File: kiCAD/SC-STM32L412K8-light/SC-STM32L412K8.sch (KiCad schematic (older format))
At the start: 66 parts, among them J1 usb, J10 Buzzer, J11 Vibro, J12 +3v, J13 +vibro, J2 +29.6 SiPM, J3 TxD (20), J4 RxD (19), J5 SWDIO, J6 SWCLK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

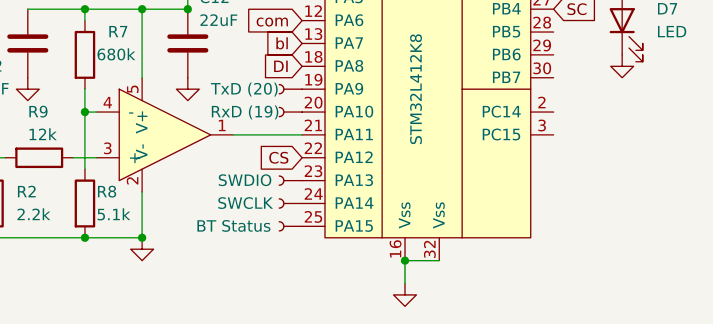
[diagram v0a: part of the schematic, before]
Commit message: modified:   kiCAD/SC-STM32L412K8-light/SC-STM32L412K8.sch 	modified:   kiCAD/SC-STM32L412K8-light/SC-STM32L412K8.sch-bak
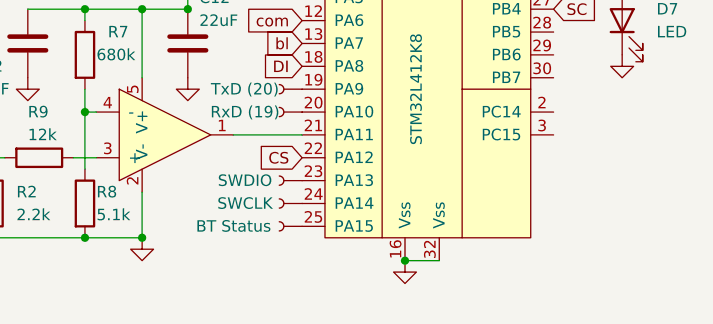
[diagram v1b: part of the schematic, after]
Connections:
- wire segments 124 -> 123
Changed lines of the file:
@@
 L power:GND #PWR012
 U 1 1 60366E3E
-P 7300 5700
-F 0 "#PWR012" H 7300 5450 50  0001 C CNN
-F 1 "GND" H 7305 5527 50  0001 C CNN
-F 2 "" H 7300 5700 50  0001 C CNN
-F 3 "" H 7300 5700 50  0001 C CNN
-	1    7300 5700
+P 7300 5600
+F 0 "#PWR012" H 7300 5350 50  0001 C CNN
+F 1 "GND" H 7305 5427 50  0001 C CNN
+F 2 "" H 7300 5600 50  0001 C CNN
+F 3 "" H 7300 5600 50  0001 C CNN
+	1    7300 5600
 	1    0    0    -1
 $EndComp
 Wire Wire Line
 	7450 5600 7300 5600
-Wire Wire Line
-	7300 5600 7300 5700
-Connection ~ 7300 5600
 $Comp
 L Device:L L4
@@
 Text GLabel 6850 5150 0    50   Input ~ 0
 CS
+Connection ~ 7300 5600
 $EndSCHEMATC

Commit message: изменено:      Android/AndroidDoZer/app/src/main/java/ru/starline/dozer/FullscreenActivity.java 	изменено:      Android/AndroidDoZer/app/src/main/res/values/strings.xml 	изменено:      kiCAD/SC-STM32L412K8-light/SC-STM32L412K8.sch 	изменено:      kiCAD/SC-STM32L412K8-light/SC-STM32L412K8.sch-bak 	изменено:      stm32Cube/STM32L412K8code/Core/Src/main.c 	изменено:      stm32Cube/STM32L412K8code/Core/Src/stm32l4xx_it.c 	изменено:      stm32Cube/STM32L412K8code/Release/Core/Src/main.o 	изменено:      stm32Cube/STM32L412K8code/Release/Core/Src/main.su 	изменено:      stm32Cube/STM32L412K8code/Release/Core/Src/stm32l4xx_it.o 	изменено:      stm32Cube/STM32L412K8code/Release/STM32L412K8.bin 	изменено:      stm32Cube/STM32L412K8code/Release/STM32L412K8.elf 	изменено:      stm32Cube/STM32L412K8code/Release/STM32L412K8.list 	изменено:      stm32Cube/STM32L412K8code/Release/STM32L412K8.map 	изменено:      stm32Cube/STM32L412K8code/STM32L412K8.ioc
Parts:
- Q1, Q2: value IRLML6344 -> IRLML0060RTPbF
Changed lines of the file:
@@
 P 4550 4350
 F 0 "Q1" H 4756 4396 50  0000 L CNN
-F 1 "IRLML6344" H 4756 4305 50  0000 L CNN
+F 1 "IRLML0060RTPbF" H 4756 4305 50  0000 L CNN
 F 2 "Package_TO_SOT_SMD:SOT-23" H 4750 4275 50  0001 L CIN
 F 3 "https://www.fairchildsemi.com/datasheets/2N/2N7002.pdf" H 4550 4350 50  0001 L CNN
@@
 P 4550 5200
 F 0 "Q2" H 4756 5246 50  0000 L CNN
-F 1 "IRLML6344" H 4756 5155 50  0000 L CNN
+F 1 "IRLML0060RTPbF" H 4756 5155 50  0000 L CNN
 F 2 "Package_TO_SOT_SMD:SOT-23" H 4750 5125 50  0001 L CIN
 F 3 "https://www.fairchildsemi.com/datasheets/2N/2N7002.pdf" H 4550 5200 50  0001 L CNN

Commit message: modified:   kiCAD/SC-STM32L412K8-light/SC-STM32L412K8.kicad_pcb 	modified:   kiCAD/SC-STM32L412K8-light/SC-STM32L412K8.kicad_pcb-bak 	modified:   kiCAD/SC-STM32L412K8-light/SC-STM32L412K8.sch 	modified:   kiCAD/SC-STM32L412K8-light/SC-STM32L412K8.sch-bak
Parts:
- L1: value LQM21FN100N -> L1 LQM21FN100N
- L2: value LQH31MN220J03L -> L2 LQH31MN220J03L
- L3: value MLZ2012M470WT000 -> L3 MLZ2012M470WT000
- L4: value MLZ2012M470WT000 -> L4 MLZ2012M470WT000
- R17: value 10M -> 30M
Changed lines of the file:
@@
 P 4600 1300
 F 0 "L2" V 4700 1300 50  0000 C CNN
-F 1 "LQH31MN220J03L" V 4800 1300 50  0000 C CNN
+F 1 "L2 LQH31MN220J03L" V 5300 1350 50  0000 C CNN
 F 2 "Inductor_SMD:L_1210_3225Metric" H 4600 1300 50  0001 C CNN
 F 3 "~" H 4600 1300 50  0001 C CNN
@@
 U 1 1 6037B2E7
 P 7500 3550
-F 0 "L4" H 7450 3900 50  0000 L CNN
-F 1 "MLZ2012M470WT000" H 7450 3800 50  0000 L CNN
+F 0 "L4" H 7350 3550 50  0000 L CNN
+F 1 "L4 MLZ2012M470WT000" H 6800 6500 50  0000 L CNN
 F 2 "Inductor_SMD:L_0805_2012Metric" H 7500 3550 50  0001 C CNN
 F 3 "~" H 7500 3550 50  0001 C CNN
@@
 P 5000 3450
 F 0 "U3" H 5050 2950 50  0000 L CNN
-F 1 "MCP73831" H 4900 2850 50  0000 L CNN
+F 1 "MCP73831" H 5000 2850 50  0000 L CNN
 F 2 "Package_TO_SOT_SMD:TSOT-23-5" H 5000 2950 50  0001 C CNN
 F 3 "http://cds.linear.com/docs/en/datasheet/405442xf.pdf" H 5000 3350 50  0001 C CNN
@@
 U 1 1 60436BF5
 P 4100 1300
-F 0 "L1" V 4300 1450 50  0000 C CNN
-F 1 "LQM21FN100N" V 4200 1200 50  0000 C CNN
+F 0 "L1" V 4200 1300 50  0000 C CNN
+F 1 "L1 LQM21FN100N" V 4800 0   50  0000 C CNN
 F 2 "Inductor_SMD:L_0805_2012Metric" H 4100 1300 50  0001 C CNN
 F 3 "~" H 4100 1300 50  0001 C CNN
@@
 U 1 1 60437DE2
 P 5600 1300
-F 0 "L3" V 5500 1300 50  0000 C CNN
-F 1 "MLZ2012M470WT000" V 5750 1000 50  0000 C CNN
+F 0 "L3" V 5700 1300 50  0000 C CNN
+F 1 "L3 MLZ2012M470WT000" V 6300 650 50  0000 C CNN
 F 2 "Inductor_SMD:L_0805_2012Metric" H 5600 1300 50  0001 C CNN
 F 3 "MLZ2012M470WT000" H 5600 1300 50  0001 C CNN
@@
 P 6500 1300
 F 0 "J2" H 6442 1075 50  0001 C CNN
-F 1 "+29.6 SiPM" H 6600 1400 50  0000 C CNN
+F 1 "+29.6 SiPM" H 6350 1400 50  0000 C CNN
 F 2 "My-library:SMD-CONN" H 6500 1300 50  0001 C CNN
 F 3 "~" H 6500 1300 50  0001 C CNN
@@
 Wire Wire Line
 	5500 5150 5500 5100
-Text Notes 5400 750  0    50   ~ 0
+Text Notes 4150 750  0    50   ~ 0
 C6, C7, C8, C11, C14 GRM21BC8YA106KE11L
 Wire Wire Line
@@
 U 1 1 609A9FBA
 P 4550 4350
-F 0 "Q1" H 4756 4396 50  0000 L CNN
-F 1 "IRLML0060RTPbF" H 4756 4305 50  0000 L CNN
+F 0 "Q1" H 4400 4600 50  0000 L CNN
+F 1 "IRLML0060RTPbF" H 3900 4500 50  0000 L CNN
 F 2 "Package_TO_SOT_SMD:SOT-23" H 4750 4275 50  0001 L CIN
 F 3 "https://www.fairchildsemi.com/datasheets/2N/2N7002.pdf" H 4550 4350 50  0001 L CNN
@@
 U 1 1 609E193B
 P 4550 5200
-F 0 "Q2" H 4756 5246 50  0000 L CNN
-F 1 "IRLML0060RTPbF" H 4756 5155 50  0000 L CNN
+F 0 "Q2" H 4400 5450 50  0000 L CNN
+F 1 "IRLML0060RTPbF" H 3900 5350 50  0000 L CNN
 F 2 "Package_TO_SOT_SMD:SOT-23" H 4750 5125 50  0001 L CIN
 F 3 "https://www.fairchildsemi.com/datasheets/2N/2N7002.pdf" H 4550 5200 50  0001 L CNN
@@
 P 7850 1900
 F 0 "R17" V 7750 1900 50  0000 C CNN
-F 1 "10M" V 7650 1900 50  0000 C CNN
+F 1 "30M" V 7650 1900 50  0000 C CNN
 F 2 "Resistor_SMD:R_0603_1608Metric" V 7780 1900 50  0001 C CNN
 F 3 "~" H 7850 1900 50  0001 C CNN

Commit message: modified:   kiCAD/SC-STM32L412K8-light/SC-STM32L412K8.kicad_pcb 	modified:   kiCAD/SC-STM32L412K8-light/SC-STM32L412K8.kicad_pcb-bak 	modified:   kiCAD/SC-STM32L412K8-light/SC-STM32L412K8.sch 	modified:   kiCAD/SC-STM32L412K8-light/SC-STM32L412K8.sch-bak
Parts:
- added J14: gndBT, My-library:SMD-CONN, symbol SC-STM32L412K8-rescue:Conn-My_Library-SC-STM32L412K8-rescue-SC-STM32L412K8-resc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
- added J15: -BAT, My-library:SMD-CONN, symbol SC-STM32L412K8-rescue:Conn-My_Library-SC-STM32L412K8-rescue-SC-STM32L412K8-resc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
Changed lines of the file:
@@
 CS
 Connection ~ 7300 5600
+$Comp
+L SC-STM32L412K8-rescue:Conn-My_Library-SC-STM32L412K8-rescue-SC-STM32L412K8-rescue-SC-STM32L412K8-rescue J14
+U 1 1 61532825
+P 5000 4300
+F 0 "J14" H 4942 4075 50  0001 C CNN
+F 1 "gndBT" V 5050 4350 50  0000 C CNN
+F 2 "My-library:SMD-CONN" H 5000 4300 50  0001 C CNN
+F 3 "~" H 5000 4300 50  0001 C CNN
+	1    5000 4300
+	0    -1   -1   0
+$EndComp
+$Comp
+L SC-STM32L412K8-rescue:Conn-My_Library-SC-STM32L412K8-rescue-SC-STM32L412K8-rescue-SC-STM32L412K8-rescue J15
+U 1 1 61533860
+P 5150 4300
+F 0 "J15" H 5092 4075 50  0001 C CNN
+F 1 "-BAT" V 5200 4200 50  0000 C CNN
+F 2 "My-library:SMD-CONN" H 5150 4300 50  0001 C CNN
+F 3 "~" H 5150 4300 50  0001 C CNN
+	1    5150 4300
+	0    -1   -1   0
+$EndComp
+$Comp
+L power:GND #PWR0108
+U 1 1 61534211
+P 5000 4400
+F 0 "#PWR0108" H 5000 4150 50  0001 C CNN
+F 1 "GND" H 5005 4227 50  0001 C CNN
+F 2 "" H 5000 4400 50  0001 C CNN
+F 3 "" H 5000 4400 50  0001 C CNN
+	1    5000 4400
+	1    0    0    -1
+$EndComp
+$Comp
+L power:GND #PWR0109
+U 1 1 61534DF7
+P 5150 4400
+F 0 "#PWR0109" H 5150 4150 50  0001 C CNN
+F 1 "GND" H 5155 4227 50  0001 C CNN
+F 2 "" H 5150 4400 50  0001 C CNN
+F 3 "" H 5150 4400 50  0001 C CNN
+	1    5150 4400
+	1    0    0    -1
+$EndComp
 $EndSCHEMATC

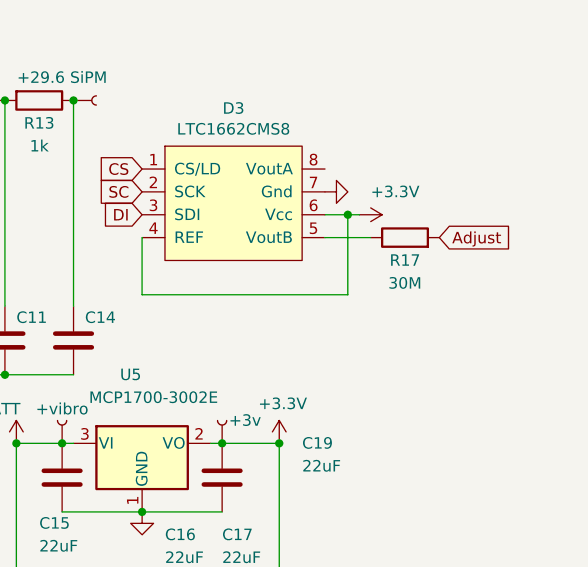
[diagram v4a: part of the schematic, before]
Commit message: изменено:      kiCAD/SC-STM32L412K8-light/SC-STM32L412K8.sch 	изменено:      kiCAD/SC-STM32L412K8-light/SC-STM32L412K8.sch-bak 	изменено:      kiCAD/SC-STM32L412K8-light/bom/ibom.html.gz
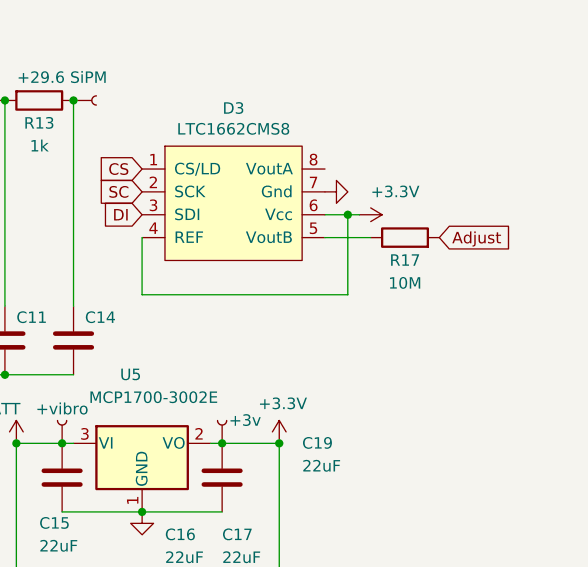
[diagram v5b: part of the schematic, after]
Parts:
- R17: value 30M -> 10M
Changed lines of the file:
@@
 P 7850 1900
 F 0 "R17" V 7750 1900 50  0000 C CNN
-F 1 "30M" V 7650 1900 50  0000 C CNN
+F 1 "10M" V 7650 1900 50  0000 C CNN
 F 2 "Resistor_SMD:R_0603_1608Metric" V 7780 1900 50  0001 C CNN
 F 3 "~" H 7850 1900 50  0001 C CNN

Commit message: изменено:      kiCAD/SC-STM32L412K8-light/SC-STM32L412K8.kicad_pcb 	изменено:      kiCAD/SC-STM32L412K8-light/SC-STM32L412K8.kicad_pcb-bak 	изменено:      kiCAD/SC-STM32L412K8-light/SC-STM32L412K8.sch 	изменено:      kiCAD/SC-STM32L412K8-light/SC-STM32L412K8.sch-bak 	изменено:      kiCAD/SC-STM32L412K8-light/bom/ibom.html.gz
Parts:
- C1, C12, C13, C15, C16, C17, C18, C19, C2, C3, C4: value 22uF -> GRM21BR60J226M
- C11, C14, C6, C7, C8: value C3216X7R1H106K160AC -> GRM21BC8YA106KE11L
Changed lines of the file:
@@
 P 7700 3750
 F 0 "C18" V 7450 3750 50  0000 C CNN
-F 1 "22uF" V 7550 3750 50  0000 C CNN
+F 1 "GRM21BR60J226M" V 7550 3750 50  0000 C CNN
 F 2 "Capacitor_SMD:C_0805_2012Metric" H 7738 3600 50  0001 C CNN
 F 3 "~" H 7700 3750 50  0001 C CNN
@@
 P 7150 3550
 F 0 "C17" H 7050 3900 50  0000 L CNN
-F 1 "22uF" H 7050 3800 50  0000 L CNN
+F 1 "GRM21BR60J226M" H 7050 3800 50  0000 L CNN
 F 2 "Capacitor_SMD:C_0805_2012Metric" H 7188 3400 50  0001 C CNN
 F 3 "~" H 7150 3550 50  0001 C CNN
@@
 P 6950 3550
 F 0 "C16" H 6800 3900 50  0000 L CNN
-F 1 "22uF" H 6800 3800 50  0000 L CNN
+F 1 "GRM21BR60J226M" H 6800 3800 50  0000 L CNN
 F 2 "Capacitor_SMD:C_0805_2012Metric" H 6988 3400 50  0001 C CNN
 F 3 "~" H 6950 3550 50  0001 C CNN
@@
 P 5550 3750
 F 0 "C13" H 5350 3850 50  0000 L CNN
-F 1 "22uF" H 5300 3650 50  0000 L CNN
+F 1 "GRM21BR60J226M" H 5300 3650 50  0000 L CNN
 F 2 "Capacitor_SMD:C_0805_2012Metric" H 5588 3600 50  0001 C CNN
 F 3 "~" H 5550 3750 50  0001 C CNN
@@
 P 5400 2350
 F 0 "C7" H 5350 2250 50  0000 R CNN
-F 1 "C3216X7R1H106K160AC" H 6050 2600 50  0001 R CNN
+F 1 "GRM21BC8YA106KE11L" H 6050 2600 50  0001 R CNN
 F 2 "Capacitor_SMD:C_0805_2012Metric" H 5438 2200 50  0001 C CNN
 F 3 "~" H 5400 2350 50  0001 C CNN
@@
 P 4300 2350
 F 0 "C3" H 4200 2300 50  0000 R CNN
-F 1 "22uF" H 4200 2400 50  0000 R CNN
+F 1 "GRM21BR60J226M" H 4200 2400 50  0000 R CNN
 F 2 "Capacitor_SMD:C_0805_2012Metric" H 4338 2200 50  0001 C CNN
 F 3 "~" H 4300 2350 50  0001 C CNN
@@
 P 3900 2350
 F 0 "C1" H 3850 2150 50  0000 R CNN
-F 1 "22uF" H 3850 2250 50  0000 R CNN
+F 1 "GRM21BR60J226M" H 3850 2250 50  0000 R CNN
 F 2 "Capacitor_SMD:C_0805_2012Metric" H 3938 2200 50  0001 C CNN
 F 3 "GRM21BR60J226M" H 3900 2350 50  0001 C CNN
@@
 P 5800 2350
 F 0 "C8" H 5750 2250 50  0000 R CNN
-F 1 "C3216X7R1H106K160AC" H 6950 2800 50  0001 R CNN
+F 1 "GRM21BC8YA106KE11L" H 6950 2800 50  0001 R CNN
 F 2 "Capacitor_SMD:C_0805_2012Metric" H 5838 2200 50  0001 C CNN
 F 3 "~" H 5800 2350 50  0001 C CNN
@@
 P 6100 2350
 F 0 "C11" H 6050 2250 50  0000 R CNN
-F 1 "C3216X7R1H106K160AC" H 7550 2900 50  0001 R CNN
+F 1 "GRM21BC8YA106KE11L" H 7550 2900 50  0001 R CNN
 F 2 "Capacitor_SMD:C_0805_2012Metric" H 6138 2200 50  0001 C CNN
 F 3 "~" H 6100 2350 50  0001 C CNN
@@
 P 6400 2350
 F 0 "C14" H 6350 2250 50  0000 R CNN
-F 1 "C3216X7R1H106K160AC" H 8150 3000 50  0001 R CNN
+F 1 "GRM21BC8YA106KE11L" H 8150 3000 50  0001 R CNN
 F 2 "Capacitor_SMD:C_0805_2012Metric" H 6438 2200 50  0001 C CNN
 F 3 "~" H 6400 2350 50  0001 C CNN
@@
 P 7050 2950
 F 0 "C19" H 7400 3100 50  0000 L CNN
-F 1 "22uF" H 7400 3000 50  0000 L CNN
+F 1 "GRM21BR60J226M" H 7400 3000 50  0000 L CNN
 F 2 "Capacitor_SMD:C_0805_2012Metric" H 7088 2800 50  0001 C CNN
 F 3 "~" H 7050 2950 50  0001 C CNN
@@
 P 6350 2950
 F 0 "C15" H 6250 2750 50  0000 L CNN
-F 1 "22uF" H 6250 2650 50  0000 L CNN
+F 1 "GRM21BR60J226M" H 6250 2650 50  0000 L CNN
 F 2 "Capacitor_SMD:C_0805_2012Metric" H 6388 2800 50  0001 C CNN
 F 3 "~" H 6350 2950 50  0001 C CNN
@@
 P 5650 4650
 F 0 "C2" H 5450 4550 50  0000 L CNN
-F 1 "22uF" H 5400 4450 50  0000 L CNN
+F 1 "GRM21BR60J226M" H 5400 4450 50  0000 L CNN
 F 2 "Capacitor_SMD:C_0805_2012Metric" H 5688 4500 50  0001 C CNN
 F 3 "~" H 5650 4650 50  0001 C CNN
@@
 P 6350 4650
 F 0 "C12" H 6400 4850 50  0000 L CNN
-F 1 "22uF" H 6400 4750 50  0000 L CNN
+F 1 "GRM21BR60J226M" H 6400 4750 50  0000 L CNN
 F 2 "Capacitor_SMD:C_0805_2012Metric" H 6388 4500 50  0001 C CNN
 F 3 "~" H 6350 4650 50  0001 C CNN
@@
 P 5600 2350
 F 0 "C6" H 5550 2250 50  0000 R CNN
-F 1 "C3216X7R1H106K160AC" H 6550 2700 50  0001 R CNN
+F 1 "GRM21BC8YA106KE11L" H 6550 2700 50  0001 R CNN
 F 2 "Capacitor_SMD:C_0805_2012Metric" H 5638 2200 50  0001 C CNN
 F 3 "~" H 5600 2350 50  0001 C CNN
@@
 P 5450 3000
 F 0 "C4" H 5400 2800 50  0000 R CNN
-F 1 "22uF" H 5400 2900 50  0000 R CNN
+F 1 "GRM21BR60J226M" H 5400 2900 50  0000 R CNN
 F 2 "Capacitor_SMD:C_0805_2012Metric" H 5488 2850 50  0001 C CNN
 F 3 "~" H 5450 3000 50  0001 C CNN

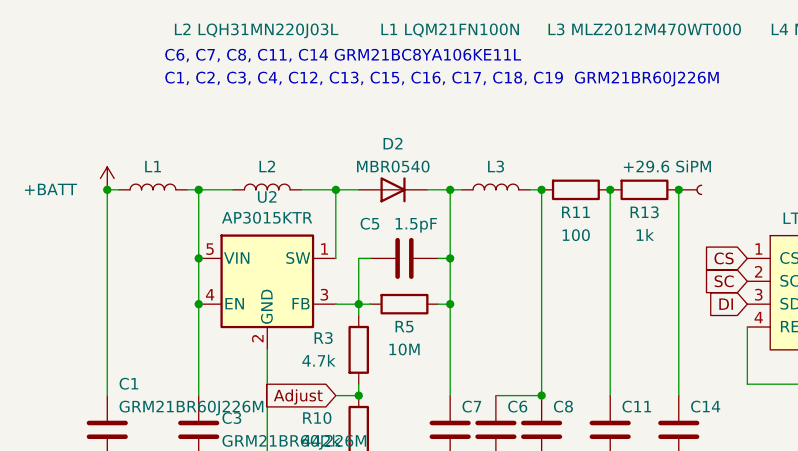
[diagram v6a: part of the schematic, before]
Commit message: изменено:      kiCAD/SC-STM32L412K8-light/SC-STM32L412K8.sch 	изменено:      kiCAD/SC-STM32L412K8-light/SC-STM32L412K8.sch-bak
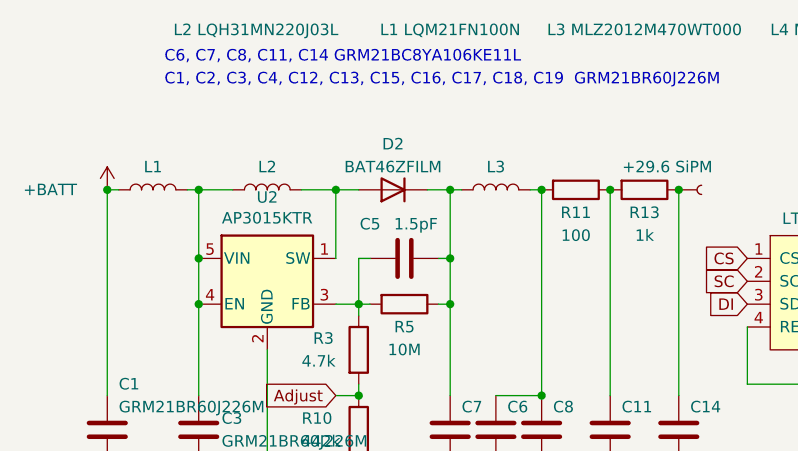
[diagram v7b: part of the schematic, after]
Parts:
- D2: value MBR0540 -> BAT46ZFILM
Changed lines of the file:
@@
 P 5150 1300
 F 0 "D2" H 5150 1100 50  0000 C CNN
-F 1 "MBR0540" H 5150 1200 50  0000 C CNN
+F 1 "BAT46ZFILM" H 5150 1200 50  0000 C CNN
 F 2 "Diode_SMD:D_SOD-123" H 5150 1300 50  0001 C CNN
 F 3 "~" H 5150 1300 50  0001 C CNN
